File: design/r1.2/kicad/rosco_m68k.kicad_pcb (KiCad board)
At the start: 4 copper layers, 160 x 100 mm, 70 parts, among them IC1 MC68010P10, IC2 ATF16V8BQL-15PU, IC4 MC68901P, IC5 ATF16V8BQL, IC6 74174N, IC8 555N, IC9 74LS01N, J1 PWR, J2 Conn_01x06, J3 Conn_02x32_Odd_Even, J5 GPIO-PANEL, Q1 3.6864MHz, Q2 5H8ET-10.000, Q3 5H8ET-4.000, U1 AT28C256-15PU, U2 AT28C256-15PU, U3 AS6C4008-55PCN, U4 AS6C4008-55PCN

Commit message: Layout for 1.2 and PLD changes for same
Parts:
- removed the C19 at (129.0, 167.7)
- removed the C24 at (129.0, 171.9)
- removed the R16 at (212.3, 97.3)
- added C13: 100nF, rosco_m68k:C2.5-3, F.Cu at (172.0, 69.7)
- added C25: 100nF, rosco_m68k:C2.5-3, F.Cu at (203.4, 72.9)
- added C26: 100nF, rosco_m68k:C2.5-3, F.Cu at (124.8, 106.1)
- added IC3: ATF16V8BQL, rosco_m68k:DIL20, F.Cu at (149.8, 94.0)
- added OSHW_Mono_0.25_Scale: UK000006, rosco_m68k:OSHW_Mono_0.25_Scale, B.Cu at (119.7, 69.2)
- added R10: 4K7, rosco_m68k:0207_10, F.Cu at (130.1, 73.7)
- added R18: 4K7, rosco_m68k:0207_10, F.Cu at (201.3, 142.9)
- added R9: 4K7, rosco_m68k:0207_10, F.Cu at (104.5, 73.6)
- added roscologo: SM-rosco_m68k_logo, rosco_m68k:SM-rosco_m68k_logo, F.Cu at (96.8, 58.1)
- added roscologo-mid: MD-rosco_m68k_logo, rosco_m68k:MD-rosco_m68k_logo, F.Cu at (152.9, 107.0)
- moved C19 141.7 mm to (212.7, 106.2)
- moved C18 140.1 mm to (212.7, 97.9)
- moved C12 135.0 mm to (172.0, 64.2), turned to 270 degrees
- moved C20 120.0 mm to (171.0, 57.4)
- moved C16 116.8 mm to (224.3, 142.9)
- moved C17 112.4 mm to (79.7, 59.0)
- moved C9 102.6 mm to (165.1, 94.0), turned to 270 degrees
- moved C22 102.3 mm to (194.3, 77.1)
- moved C23 99.3 mm to (180.3, 79.4)
- moved C7 94.6 mm to (114.4, 93.3), turned to 270 degrees
- moved C8 77.7 mm to (114.4, 106.1), turned to 270 degrees
- moved C24 61.1 mm to (183.7, 124.1)
- moved R8 55.8 mm to (178.8, 97.4), turned to 180 degrees
- moved IC2 54.0 mm to (99.0, 93.4)
- moved R2 48.5 mm to (188.5, 139.8), turned to 90 degrees
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- renumbered C13 to C14, C14 to C15, C15 to C16, C16 to C17, C17 to C18, C23 to C19, C18 to C20, C25 to C21, C20 to C23, C21 to C24, R9 to R11, R10 to R12, R11 to R13, R12 to R14, R13 to R15, R14 to R16, R15 to R17, R17 to R19
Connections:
- IC1 pad 45: /Expansion/A17 -> A17
- IC4 pad 17: Net-(C1-Pad1) -> Net-(C2-Pad1)
- IC4 pad 18: Net-(C2-Pad1) -> Net-(C1-Pad1)
- IC4 pad 48: IOSEL -> MFPSEL
- IC5 pad 11: GND -> A17
- IC5 pad 5: ODDRAMSEL -> EVENROMSEL
- IC5 pad 6: EVENROMSEL -> ODDRAMSEL
- J3 pad 33: /Expansion/A17 -> A17
- J5 pad 16: (no net) -> GND
- R3 pad 1: IPL2 -> VCC
- R3 pad 2: VCC -> Net-(Q2-Pad1)
- R4 pad 1: IPL1 -> IPL2
- R5 pad 1: IPL0 -> IPL1
- R6 pad 1: BR -> IPL0
- R7 pad 1: BGACK -> BR
- R8 pad 1: BERR -> VCC
- R8 pad 2: VCC -> Net-(Q3-Pad1)
- U3 pad 2: /Expansion/A17 -> A17
- U4 pad 2: /Expansion/A17 -> A17
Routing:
- net /Expansion/D5: track 0.00 -> 346.4 mm, vias 0 -> 7
- net /Expansion/D6: track 0.00 -> 341.0 mm, vias 0 -> 5
- net /Expansion/D4: track 0.00 -> 339.4 mm, vias 0 -> 6
- net /Expansion/D7: track 0.00 -> 337.9 mm, vias 0 -> 5
- net /Expansion/D3: track 0.00 -> 337.7 mm, vias 0 -> 5
- net RW: track 0.00 -> 324.8 mm, vias 0 -> 9
- net /Expansion/D2: track 0.00 -> 317.5 mm, vias 0 -> 6
- net /Expansion/D1: track 0.00 -> 315.4 mm, vias 0 -> 5
- net /Expansion/D0: track 0.00 -> 297.5 mm, vias 0 -> 5
- net RESET: track 0.00 -> 265.3 mm, vias 0 -> 5
- net /Expansion/A1: track 0.00 -> 263.9 mm, vias 0 -> 3
- net /Expansion/A5: track 0.00 -> 260.3 mm, vias 0 -> 4
- net /Expansion/A2: track 0.00 -> 251.2 mm, vias 0 -> 3
- net /Expansion/D11: track 0.00 -> 249.4 mm, vias 0 -> 4
- net /Expansion/D12: track 0.00 -> 248.6 mm, vias 0 -> 4
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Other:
- rule via_min_drill: 0.3 -> 0.25
- rule via_min_size: 0.4 -> 0.3
- board text added: "Copyright © 2020"
- board text added: "EXPANSION - SEE http://github.com/rosco-m68k/rosco_m68k"
- board text added: "GND CTS VCC RXD TXD N/C"
- board text added: "Revision 1.2 (August 2020)"
- board text added: "UART VCC"
- board text added: "revision 1.2"
- board text added: "rosco_m68k revision 1.2"
- board text removed: "CTS RXD TXD GND"
- board text removed: "EXPANSION - SEE http://github.com/roscopeco/rosco_m68k"
- board text removed: "copyright 2020"
- board text removed: "revision 1.2 (August 2020)"
- board text removed: "rosco_m68k"
- board text removed: "rosco_m68k revision one"

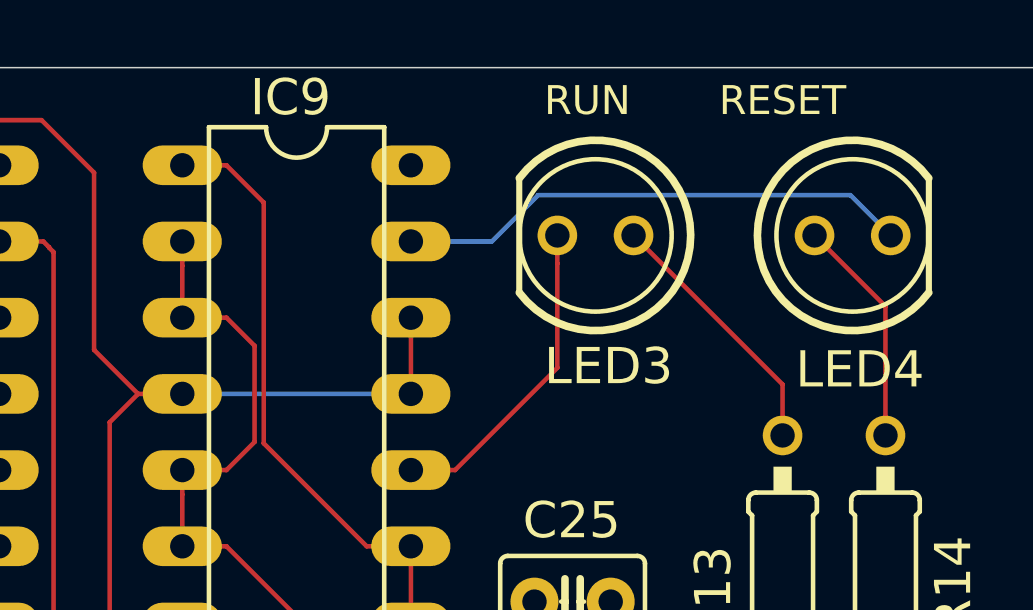
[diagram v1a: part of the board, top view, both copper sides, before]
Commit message: Fix reset LED snafu
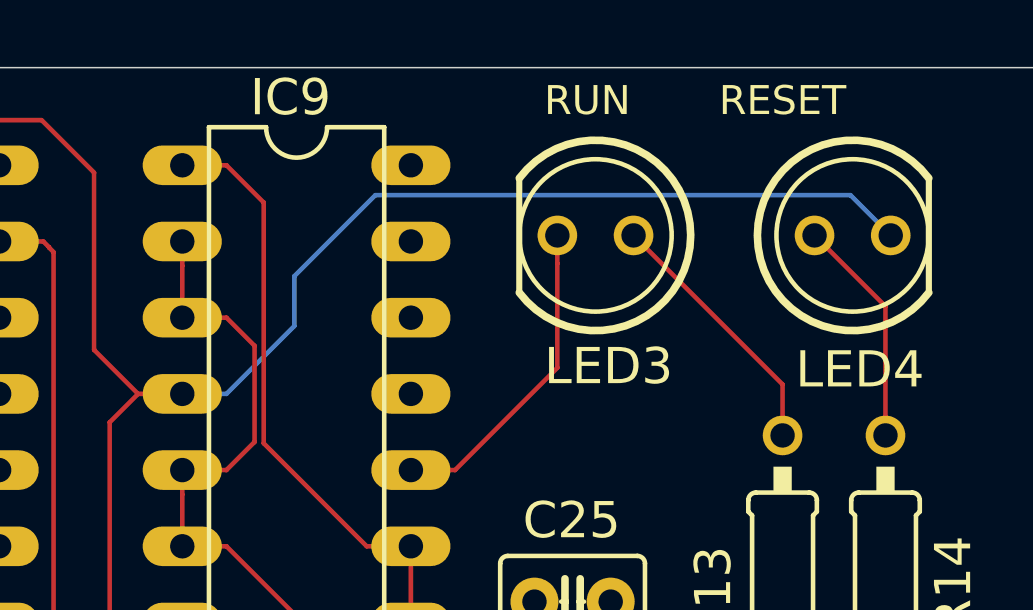
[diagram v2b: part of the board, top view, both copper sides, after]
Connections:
- IC9 pad 11: RESET -> VCC
- IC9 pad 12: RESET -> VCC
- LED4 pad K: Net-(IC9-Pad13) -> RESET
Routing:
- net RESET: track 265.3 -> 283.1 mm
- net Net-(IC9-Pad13): track 17.2 -> 0.00 mm
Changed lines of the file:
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@@
   )
   (setup
-    (last_trace_width 0.25)
+    (last_trace_width 0.85)
     (user_trace_width 0.1524)
     (user_trace_width 0.65)
@@
       (net 44 "Net-(IC9-Pad13)") (solder_mask_margin 0.1016))
     (pad 12 thru_hole oval (at -2.54 -3.81) (size 2.6416 1.3208) (drill 0.8128) (layers *.Cu *.Mask)
-      (net 7 RESET) (solder_mask_margin 0.1016))
+      (net 17 VCC) (solder_mask_margin 0.1016))
     (pad 11 thru_hole oval (at 0 -3.81) (size 2.6416 1.3208) (drill 0.8128) (layers *.Cu *.Mask)
-      (net 7 RESET) (solder_mask_margin 0.1016))
+      (net 17 VCC) (solder_mask_margin 0.1016))
     (pad 10 thru_hole oval (at 2.54 -3.81) (size 2.6416 1.3208) (drill 0.8128) (layers *.Cu *.Mask)
       (net 45 "Net-(IC9-Pad10)") (solder_mask_margin 0.1016))
@@
     (fp_line (start 2.54 1.905) (end 2.54 -1.905) (layer F.SilkS) (width 0.2032))
     (pad K thru_hole circle (at 1.27 0) (size 1.3208 1.3208) (drill 0.8128) (layers *.Cu *.Mask)
-      (net 44 "Net-(IC9-Pad13)") (solder_mask_margin 0.1016))
+      (net 7 RESET) (solder_mask_margin 0.1016))
     (pad A thru_hole circle (at -1.27 0) (size 1.3208 1.3208) (drill 0.8128) (layers *.Cu *.Mask)
       (net 46 "Net-(LED4-PadA)") (solder_mask_margin 0.1016))
@@
   (segment (start 106.221704 78.7081) (end 105.468414 77.95481) (width 0.1524) (layer Bottom) (net 6))
   (segment (start 107.2815 78.7081) (end 106.221704 78.7081) (width 0.1524) (layer Bottom) (net 6))
-  (segment (start 198.01 65.975) (end 198.01 63.435) (width 0.1524) (layer Top) (net 7))
   (segment (start 187.9701 66.9217) (end 188.9168 65.975) (width 0.1524) (layer Top) (net 7))
   (segment (start 187.9701 78.77) (end 187.9701 66.9217) (width 0.1524) (layer Top) (net 7))
@@
   (segment (start 188.9168 65.975) (end 190.39 65.975) (width 0.1524) (layer Top) (net 7))
   (segment (start 187.45 58.6) (end 187.45 64.5082) (width 0.1524) (layer Top) (net 7))
-  (segment (start 190.39 65.975) (end 198.01 65.975) (width 0.1524) (layer Bottom) (net 7))
   (via (at 188 82.25) (size 0.8) (drill 0.4) (layers Top Bottom) (net 7))
   (segment (start 188 78.7999) (end 187.9701 78.77) (width 0.1524) (layer Top) (net 7))
@@
   (segment (start 129.996231 82.843031) (end 130.21 83.0568) (width 0.1524) (layer Bottom) (net 7))
   (segment (start 101.556969 82.843031) (end 129.996231 82.843031) (width 0.1524) (layer Bottom) (net 7))
+  (segment (start 191.8632 65.975) (end 190.39 65.975) (width 0.1524) (layer Bottom) (net 7))
+  (segment (start 196.825 59.35) (end 194.125 62.05) (width 0.1524) (layer Bottom) (net 7))
+  (segment (start 194.125 63.7132) (end 191.8632 65.975) (width 0.1524) (layer Bottom) (net 7))
+  (segment (start 212.6625 59.35) (end 196.825 59.35) (width 0.1524) (layer Bottom) (net 7))
+  (segment (start 194.125 62.05) (end 194.125 63.7132) (width 0.1524) (layer Bottom) (net 7))
+  (segment (start 214.0051 60.6926) (end 212.6625 59.35) (width 0.1524) (layer Bottom) (net 7))
   (segment (start 140.3276 78.8224) (end 140.35 78.8) (width 0.1524) (layer Bottom) (net 8))
   (via (at 140.35 78.8) (size 0.8) (drill 0.4) (layers Top Bottom) (net 8))
@@
   (segment (start 197.15 83.8574) (end 198.2976 85.005) (width 0.1524) (layer Top) (net 42))
   (segment (start 197.15 76.3418) (end 197.15 83.8574) (width 0.1524) (layer Top) (net 42))
-  (segment (start 214.0051 60.6926) (end 212.6625 59.35) (width 0.1524) (layer Bottom) (net 44))
-  (segment (start 212.6625 59.35) (end 202.25 59.35) (width 0.1524) (layer Bottom) (net 44))
-  (segment (start 200.705 60.895) (end 198.01 60.895) (width 0.1524) (layer Bottom) (net 44))
-  (segment (start 202.25 59.35) (end 200.705 60.895) (width 0.1524) (layer Bottom) (net 44))
   (segment (start 202.8926 61.626546) (end 202.8926 60.6926) (width 0.1524) (layer Top) (net 45))
   (segment (start 202.8926 65.1056) (end 202.8926 61.626546) (width 0.1524) (layer Top) (net 45))

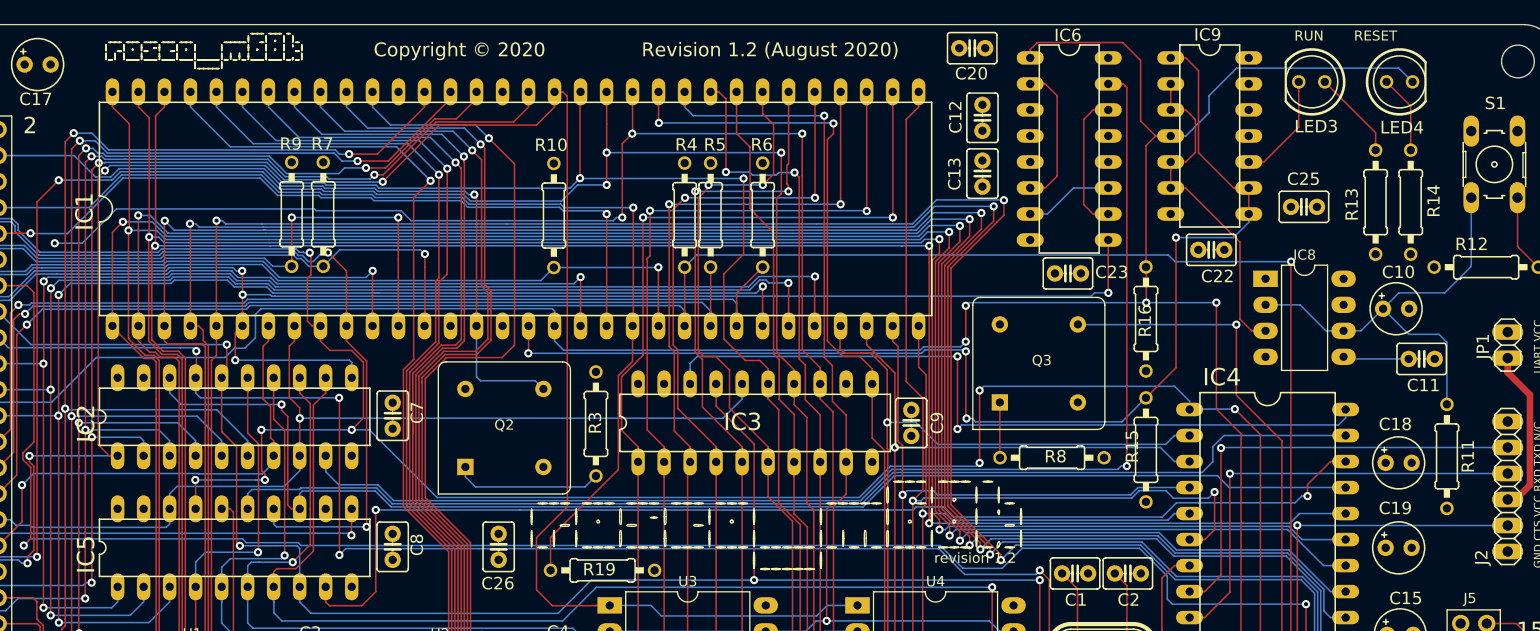
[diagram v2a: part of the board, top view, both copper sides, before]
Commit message: Add DTACK watchdog, tidy up footprints
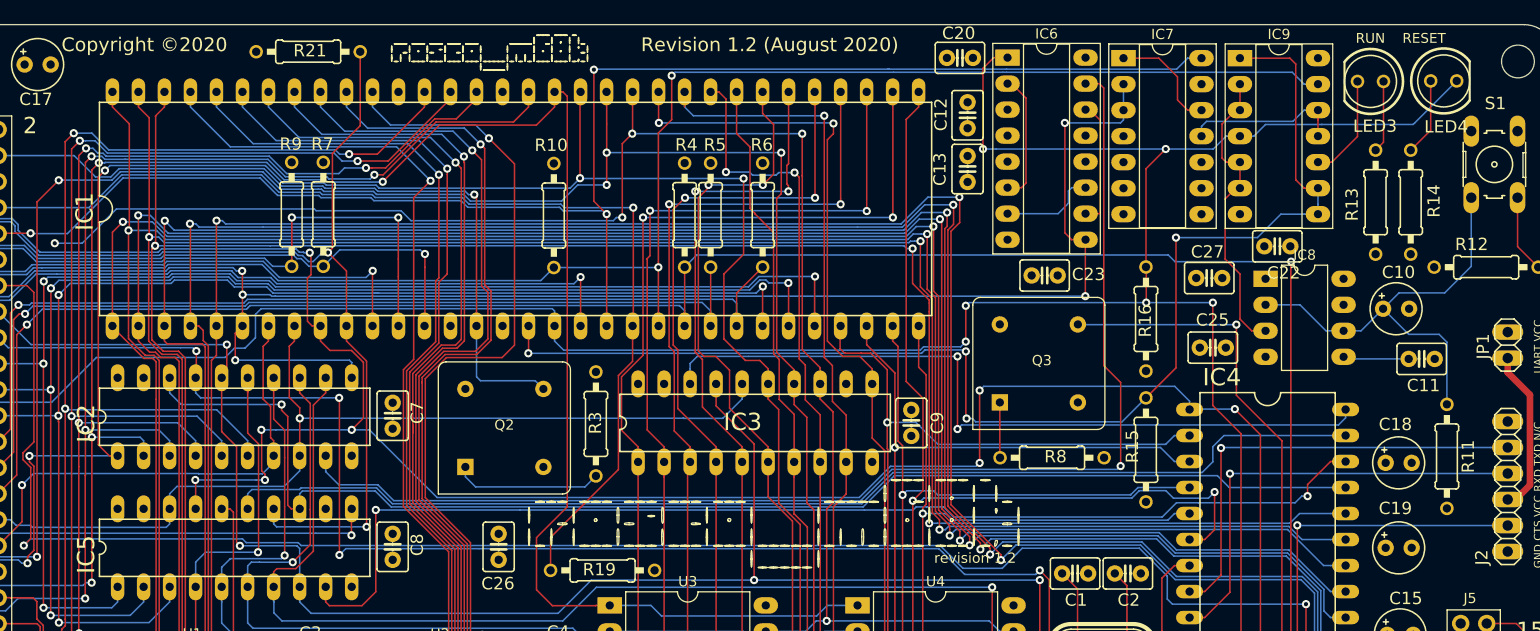
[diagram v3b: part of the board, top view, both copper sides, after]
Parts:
- removed roscologo: SM-rosco_m68k_logo, rosco_m68k:SM-rosco_m68k_logo
- removed roscologo-mid: MD-rosco_m68k_logo, rosco_m68k:MD-rosco_m68k_logo
- added C27: 100nF, rosco_m68k:C2.5-3, F.Cu at (194.2, 79.8)
- added IC7: 74LS93, Package_DIP:DIP-14_W7.62mm_Socket_LongPads, F.Cu at (185.8, 58.4)
- added R21: 4K7, rosco_m68k:0207_10, F.Cu at (106.2, 57.8)
- added REF**: MD-rosco_m68k_logo, rosco_m68k:MD-rosco_m68k_logo, F.Cu at (152.7, 106.8)
- added REF**: SM-rosco_m68k_logo, rosco_m68k:SM-rosco_m68k_logo, F.Cu at (124.7, 58.3)
- added REF**: LG-rosco_m68k_logo_rotated, rosco_m68k:LG-rosco_m68k_logo_rotated, B.Cu at (153.7, 104.2)
- IC6: footprint rosco_m68k:DIL16 -> Package_DIP:DIP-16_W7.62mm_Socket_LongPads
- IC9: footprint rosco_m68k:DIL14 -> Package_DIP:DIP-14_W7.62mm_Socket_LongPads
- moved C25 16.4 mm to (194.5, 86.7)
- moved IC6 10.8 mm to (174.4, 58.3), turned to 0 degrees
- moved IC9 8.15 mm to (197.2, 58.4), turned to 0 degrees
- moved C22 6.46 mm to (200.8, 76.8)
- moved LED3 5.74 mm to (209.9, 60.6)
- moved LED4 4.32 mm to (217.1, 60.6)
- moved C23 2.28 mm to (178.1, 79.6)
- moved C20 1.53 mm to (169.8, 58.4)
- moved C13 1.52 mm to (170.6, 69.2)
- moved C12 1.47 mm to (170.6, 64.0)
- moved OSHW_Mono_0.25_Scale 0.78 mm to (119.2, 69.8)
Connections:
- net A17 renamed /Expansion/A17
- IC9 pad 11: VCC -> Net-(IC7-Pad11)
- IC9 pad 12: VCC -> Net-(IC7-Pad11)
- IC9 pad 13: Net-(IC9-Pad13) -> BERR
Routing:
- net BERR: track 123.3 -> 206.2 mm, vias 1 -> 2
- net E: track 74.1 -> 148.7 mm, vias 2 -> 3
- net DTACK: track 141.5 -> 162.4 mm
- net AS: track 184.1 -> 204.9 mm, vias 4 -> 5
- net Net-(IC7-Pad11): track 0.00 -> 15.5 mm
- net Net-(IC7-Pad1): track 0.00 -> 11.0 mm
- net RESET: track 283.1 -> 291.8 mm, vias 5 -> 7
- net HALT: track 116.4 -> 124.6 mm
- net /Expansion/D0: track 297.5 -> 291.8 mm
- net /Expansion/D1: track 315.4 -> 310.1 mm
- net /Expansion/D2: track 317.5 -> 312.7 mm
- net /Expansion/D3: track 337.7 -> 333.8 mm
- net /Expansion/D4: track 339.4 -> 336.0 mm
- net /Expansion/D5: track 346.4 -> 343.8 mm
- net Net-(IC8-Pad3): track 33.9 -> 31.3 mm
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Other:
- board text added: "Copyright ©2020"
- board text removed: "Copyright © 2020"
